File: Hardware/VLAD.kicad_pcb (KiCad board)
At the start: 2 copper layers, 90 x 90 mm, 101 parts, among them J1 BMP388, J2 BNO055, J3 Micro_SD_Card, J4 Conn_01x02_Male, J5 Conn_01x03_Male, P1 USB_C_Plug_USB2.0, Q1 S8050, Q2 S8050, Q3 S8550, Q4 S8550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

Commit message: Some connections
I hope this is ok
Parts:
- moved SW3 8.80 mm to (86.8, 106.6), turned to 180 degrees
- moved C1.4 1.62 mm to (96.4, 48.5)
- moved Battery1 1.30 mm to (92.8, 106.6), turned to 0 degrees
- moved U4 0.91 mm to (74.3, 106.9), turned to 90 degrees
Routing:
- net Net-(C2.1-Pad1): track 11.4 -> 83.2 mm
- net +3V3: track 30.8 -> 60.9 mm
- net /usb/VBUS: track 0.00 -> 24.8 mm
- net /SDCS: track 0.00 -> 15.6 mm
- net /usb/D-: track 0.00 -> 13.0 mm
- net /usb/D+: track 0.00 -> 12.3 mm
- net Net-(SW3-Pad2): track 0.00 -> 7.85 mm
- net Net-(R16-Pad2): track 0.00 -> 6.61 mm
- net Net-(Battery1-Pad1): track 0.00 -> 6.07 mm
- net /SerialRx: track 0.00 -> 5.24 mm
- net Net-(Q3-Pad1): track 0.00 -> 4.17 mm
- net Net-(Q3-Pad2): track 0.00 -> 4.04 mm
- net /USB_RTS: track 3.07 -> 7.01 mm
- net Net-(12VBoostConverter1-Pad5): track 0.00 -> 2.95 mm
- net Net-(P1-PadA5): track 0.00 -> 2.71 mm
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
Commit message: Added lots of things - needs some redoing
Fun, but ffs could have been easier
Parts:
- removed the Q5 at (82.0, 39.0)
- removed the Q6 at (82.0, 82.0)
- removed SW3: SW_SPST, Button_Switch_THT:SW_DIP_SPSTx01_Slide_9.78x4.72mm_W7.62mm_P2.54mm
- added J6: Conn_01x02_Male, Connector_PinHeader_2.54mm:PinHeader_1x02_P2.54mm_Vertical, F.Cu at (93.0, 101.0)
- added JP1: Jumper_2_Open, Connector_PinHeader_2.54mm:PinHeader_1x02_P2.54mm_Vertical, F.Cu at (74.0, 25.0)
- Q5, Q6: footprint Package_TO_SOT_THT:TO-220-3_Vertical -> Package_TO_SOT_SMD:SOT-23
- Q7: value 2N2219 -> Q_NMOS_GDS; footprint Package_TO_SOT_THT:TO-92_Inline -> Package_TO_SOT_SMD:SOT-23
- moved J2 61.4 mm to (74.0, 128.0)
- moved J1 49.3 mm to (74.0, 133.0), turned to 90 degrees
- moved Q7 37.2 mm to (74.0, 29.0), turned to 270 degrees
- moved TP6 28.4 mm to (33.0, 99.0), turned to 270 degrees
- moved R7 26.4 mm to (33.0, 102.0)
- moved C8 22.5 mm to (57.0, 98.0), turned to 90 degrees
- moved C7 21.6 mm to (55.0, 98.0), turned to 90 degrees
- moved AE1 15.1 mm to (57.0, 105.0), turned to 0 degrees
- moved SDLED2 14.8 mm to (34.0, 92.0), turned to 270 degrees
- moved U4 14.4 mm to (87.0, 100.0)
- moved R21 13.4 mm to (81.0, 99.0), turned to 0 degrees
- moved Q4 13.3 mm to (29.0, 92.0)
- moved Q5 11.7 mm to (87.0, 38.0)
- moved R14 10.6 mm to (32.0, 92.0), turned to 90 degrees
- moved U2 8.54 mm to (45.0, 98.0), turned to 0 degrees
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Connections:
- C2.1 pad 1: Net-(C2.1-Pad1) -> Net-(C1.1-Pad1)
- J4 pad 1: GND -> Net-(J4-Pad1)
- L2 pad 1: Net-(C2.1-Pad1) -> Net-(C1.1-Pad1)
- Q7 pad 1: Net-(C1.1-Pad1) -> 12VBusSwitch
- Q7 pad 2: 12VBusSwitch -> Net-(JP1-Pad1)
- Q7 pad 3: Net-(C2.1-Pad1) -> GND
- R21 pad 2: Net-(C2.1-Pad1) -> Net-(C1.1-Pad1)
- U4 pad 5: Net-(C2.1-Pad1) -> Net-(C1.1-Pad1)
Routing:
- net Net-(C2.1-Pad1): track 83.2 -> 0.00 mm
- net Net-(C1.1-Pad1): track 21.1 -> 72.2 mm
- net +3V3: track 60.9 -> 38.5 mm
- net Net-(D2-Pad2): track 21.4 -> 0.00 mm
- net Net-(D3-Pad2): track 20.8 -> 0.00 mm
- net +12V: track 46.1 -> 27.2 mm
- net /SDA: track 17.8 -> 0.00 mm
- net /SCL: track 18.5 -> 1.25 mm
- net Net-(6VBoostConverter1-Pad8): track 16.4 -> 0.00 mm
- net Net-(12VBoostConverter1-Pad8): track 16.4 -> 0.00 mm
- net /Power/Source2: track 0.00 -> 16.4 mm
- net /Power/Drain1: track 0.00 -> 15.9 mm
- net /Power/Source1: track 0.00 -> 15.0 mm
- net /Power/Drain2: track 0.00 -> 13.2 mm
- net Net-(Q4-Pad2): track 0.00 -> 8.34 mm
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
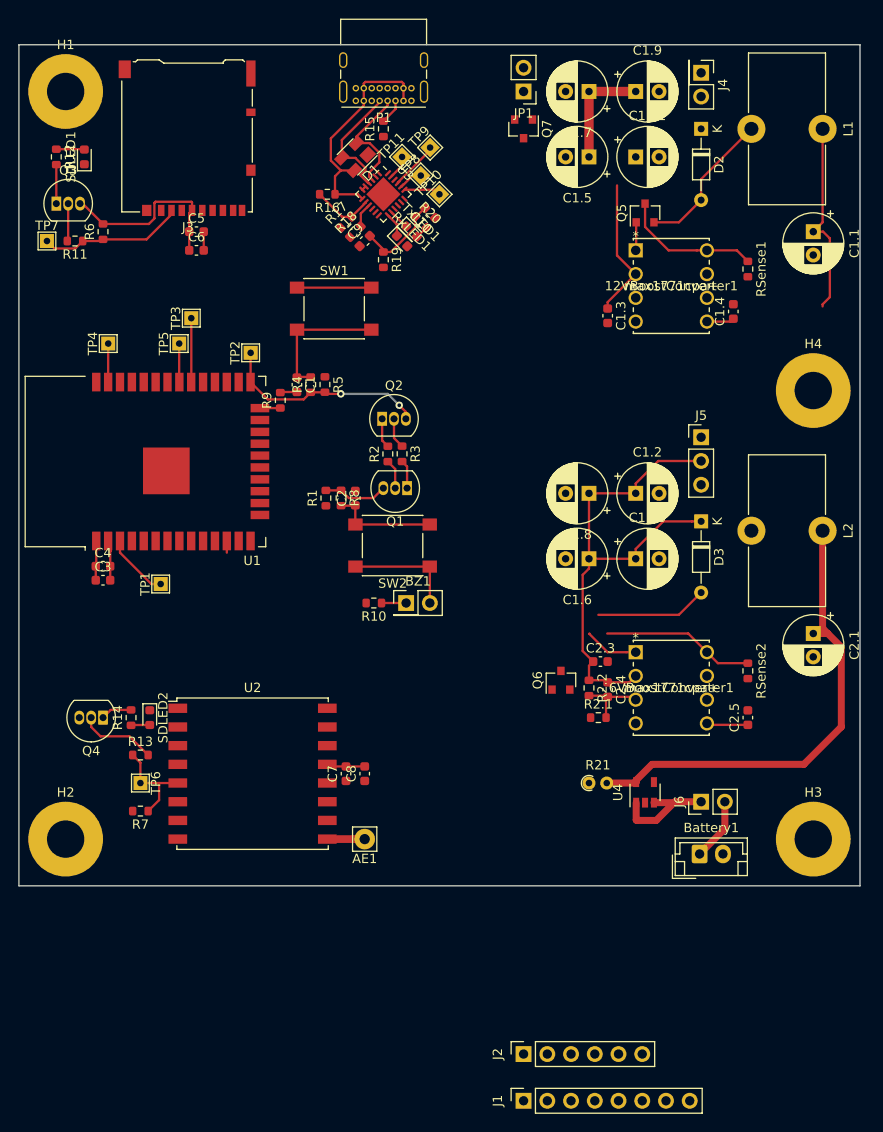
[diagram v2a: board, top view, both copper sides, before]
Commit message: Added bunch of vias
Now need to connect some more tracks up and we're good to proceed to adding ground planes etc. Also decreased the size of the board to fit within 90mm x 80mm, have further opportunities to potentially squeeze it.
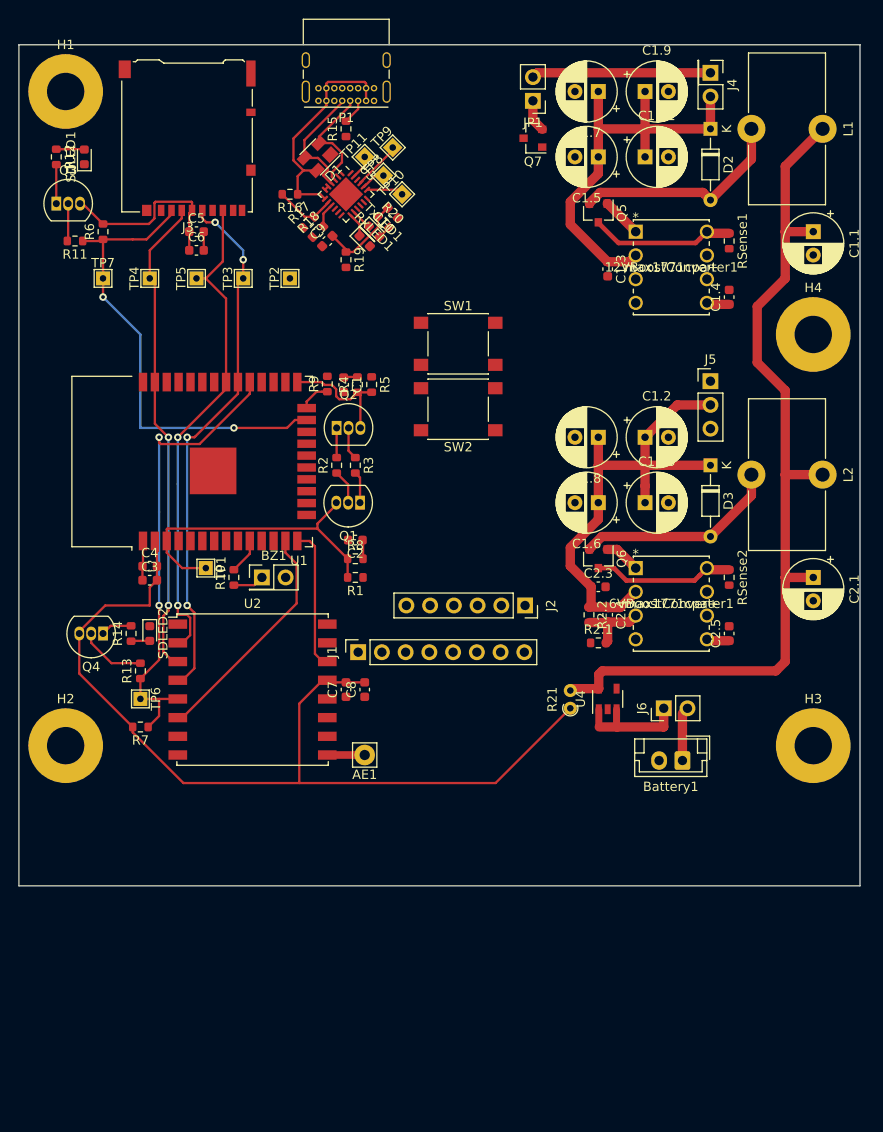
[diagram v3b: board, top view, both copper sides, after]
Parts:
- Q5, Q6: value MTP3055VL -> Q_NMOS_GDS
- moved J1 51.2 mm to (56.3, 85.0)
- moved J2 48.0 mm to (74.2, 80.0), turned to 270 degrees
- moved SW2 16.2 mm to (67.0, 59.0)
- moved BZ1 15.7 mm to (46.0, 77.0)
- moved R10 15.2 mm to (43.0, 77.0), turned to 90 degrees
- moved SW1 13.8 mm to (67.0, 52.0)
- moved Q6 13.6 mm to (82.0, 75.0), turned to 270 degrees
- moved J6 10.8 mm to (89.0, 91.0)
- moved U4 10.8 mm to (83.0, 90.0)
- moved RSense2 10.2 mm to (96.0, 77.0)
- moved Battery1 10.2 mm to (91.0, 96.6), turned to 180 degrees
- moved H2 10.0 mm to (25.0, 95.0)
- moved H3 10.0 mm to (105.0, 95.0)
- moved C2.5 9.22 mm to (96.0, 83.0)
- moved R1 9.06 mm to (56.0, 77.0), turned to 180 degrees
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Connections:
- net /Power/Drain1 renamed Net-(D2-Pad2)
- net /Power/Drain2 renamed Net-(D3-Pad2)
- net /Power/Gate1 renamed Net-(12VBoostConverter1-Pad1)
- net /Power/Gate2 renamed Net-(6VBoostConverter1-Pad1)
- net /Power/Source1 renamed Net-(12VBoostConverter1-Pad8)
- net /Power/Source2 renamed Net-(6VBoostConverter1-Pad8)
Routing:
- net +3V3: track 38.5 -> 128.3 mm
- net /SCLK: track 7.34 -> 56.9 mm, vias 0 -> 4
- net /MISO: track 4.13 -> 53.1 mm, vias 0 -> 2
- net /MOSI: track 4.63 -> 52.2 mm, vias 0 -> 2
- net /RadioCS: track 10.9 -> 50.2 mm, vias 0 -> 2
- net /SDCS: track 15.6 -> 51.1 mm, vias 0 -> 2
- net /RadioReset: track 0.00 -> 25.0 mm
- net Net-(C1.1-Pad1): track 72.2 -> 96.3 mm
- net GND: track 27.8 -> 6.71 mm
- net /EN: track 14.7 -> 34.5 mm
- net +12V: track 27.2 -> 46.9 mm
- net Net-(J4-Pad1): track 0.00 -> 19.2 mm
- net /RadioDone: track 0.50 -> 15.3 mm
- net Net-(C1-Pad1): track 14.5 -> 1.45 mm
- net Net-(C2-Pad1): track 11.5 -> 2.02 mm
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
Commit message: Not much new
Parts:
- moved J2 33.9 mm to (66.6, 113.0)
- moved J1 33.1 mm to (53.3, 118.0)
- moved SW1 10.0 mm to (57.0, 51.0)
- moved TP10 8.94 mm to (69.0, 32.0)
- moved SW2 8.06 mm to (68.0, 51.0), turned to 0 degrees
- moved TP8 6.32 mm to (65.0, 32.0)
- moved TP9 1.41 mm to (61.0, 32.0)
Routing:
- net +3V3: track 128.3 -> 236.4 mm, vias 0 -> 2
- net /USB_RTS: track 7.33 -> 65.3 mm, vias 0 -> 2
- net /SerialTx: track 2.58 -> 51.9 mm, vias 0 -> 2
- net /USB_DTR: track 6.62 -> 53.7 mm, vias 0 -> 2
- net /SerialRx: track 5.24 -> 43.7 mm, vias 0 -> 2
- net Net-(C2-Pad1): track 2.02 -> 32.7 mm
- net /IO0: track 13.7 -> 25.1 mm
- net Net-(C1-Pad1): track 1.45 -> 10.6 mm
- net Net-(R19-Pad2): track 0.00 -> 3.50 mm

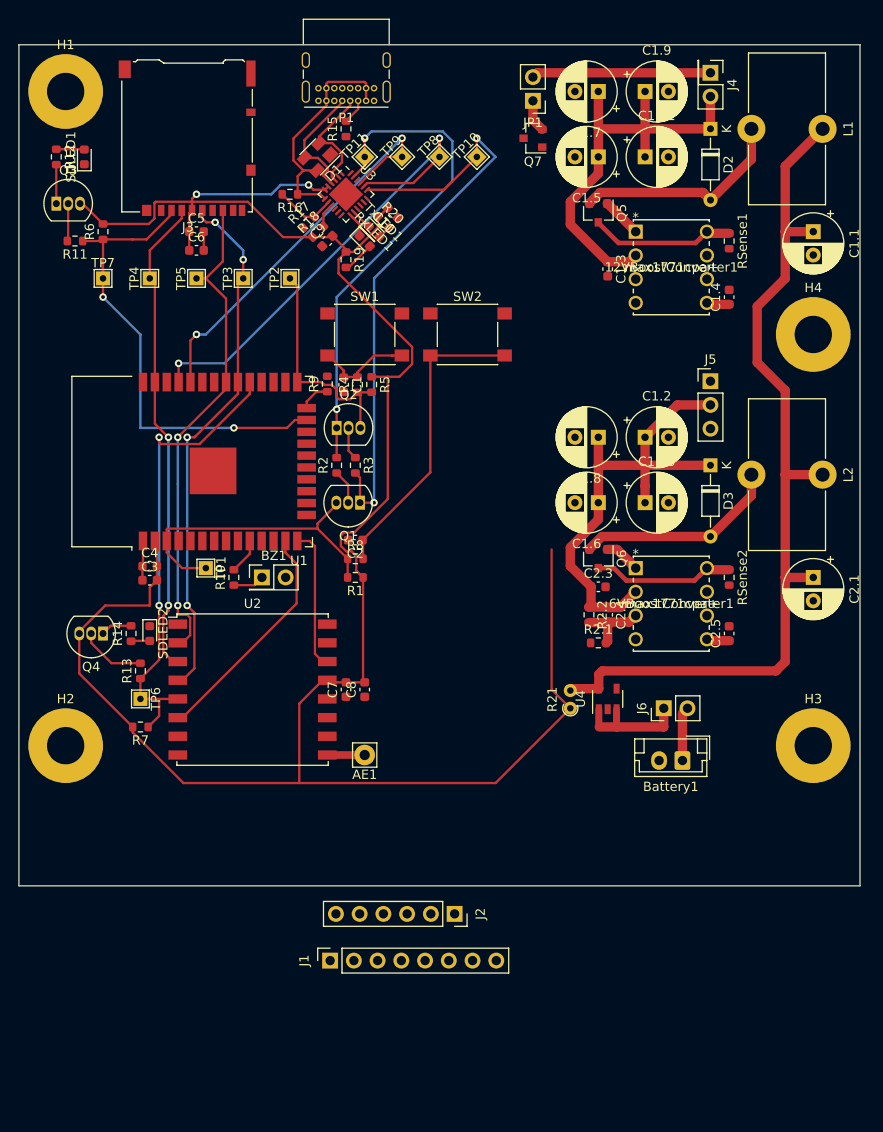
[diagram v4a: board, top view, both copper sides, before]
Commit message: Tracks done (albeit OCDifying)
All tracks are done in the sense that everything has found a routing, some components still may need to be moved though, such as the sensors on board and the push switches. 
Antenna stuff needs doing.
Board may need to be reshaped (keepout zone?).
GND plane needs to be added + silkscreens + memes
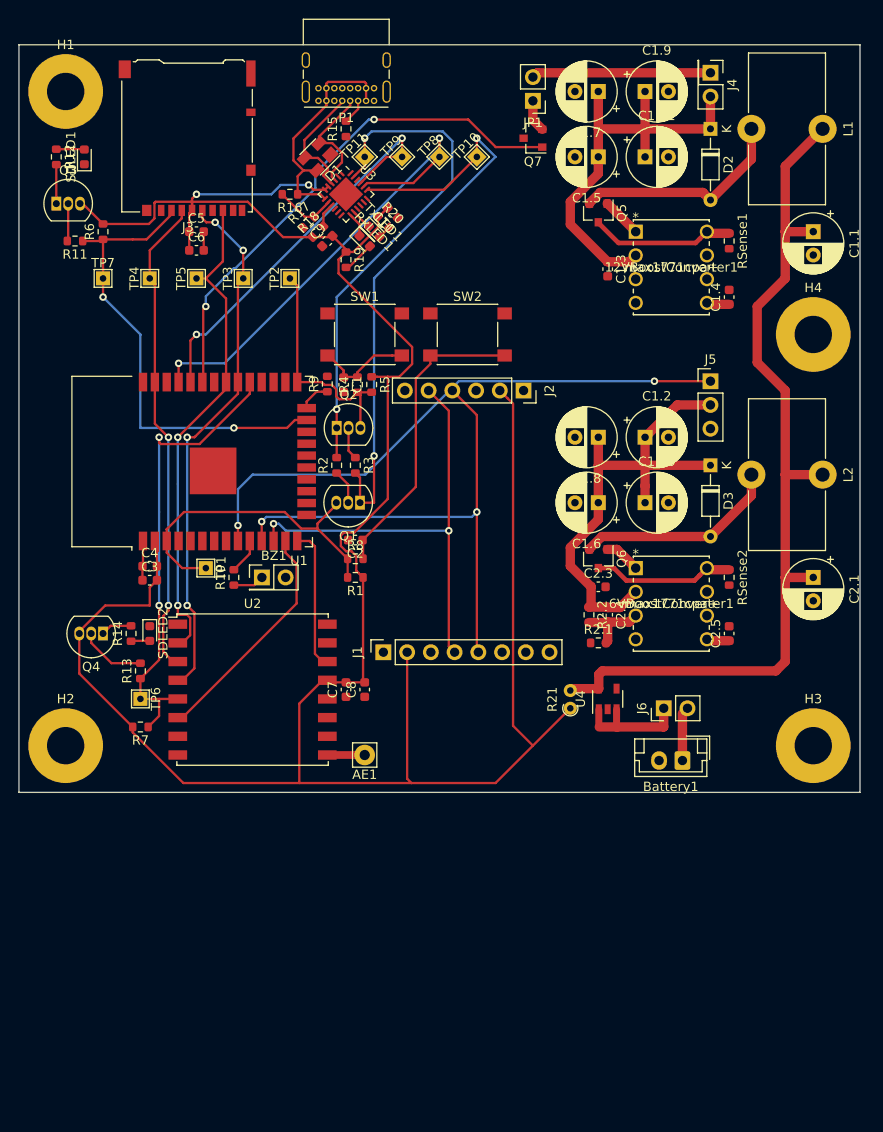
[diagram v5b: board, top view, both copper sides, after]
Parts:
- moved J2 56.5 mm to (74.0, 57.0)
- moved J1 33.5 mm to (59.0, 85.0)
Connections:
- U1 pad 33: /ServoPin -> 12VBusSwitch
- U1 pad 9: 12VBusSwitch -> /ServoPin
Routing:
- net /ServoPin: track 0.00 -> 60.9 mm, vias 0 -> 2
- net 12VBusSwitch: track 0.00 -> 55.4 mm, vias 0 -> 2
- net /SDA: track 0.00 -> 54.7 mm, vias 0 -> 2
- net /SCL: track 0.00 -> 50.1 mm, vias 0 -> 2
- net +3V3: track 236.4 -> 272.2 mm
- net /EN: track 34.5 -> 36.0 mm
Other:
- board size 90 x 90 mm -> 90 x 80 mm

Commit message: Added GND plane and 3V3 plane
4 connections left to make, not sure what the issue is with some of them...
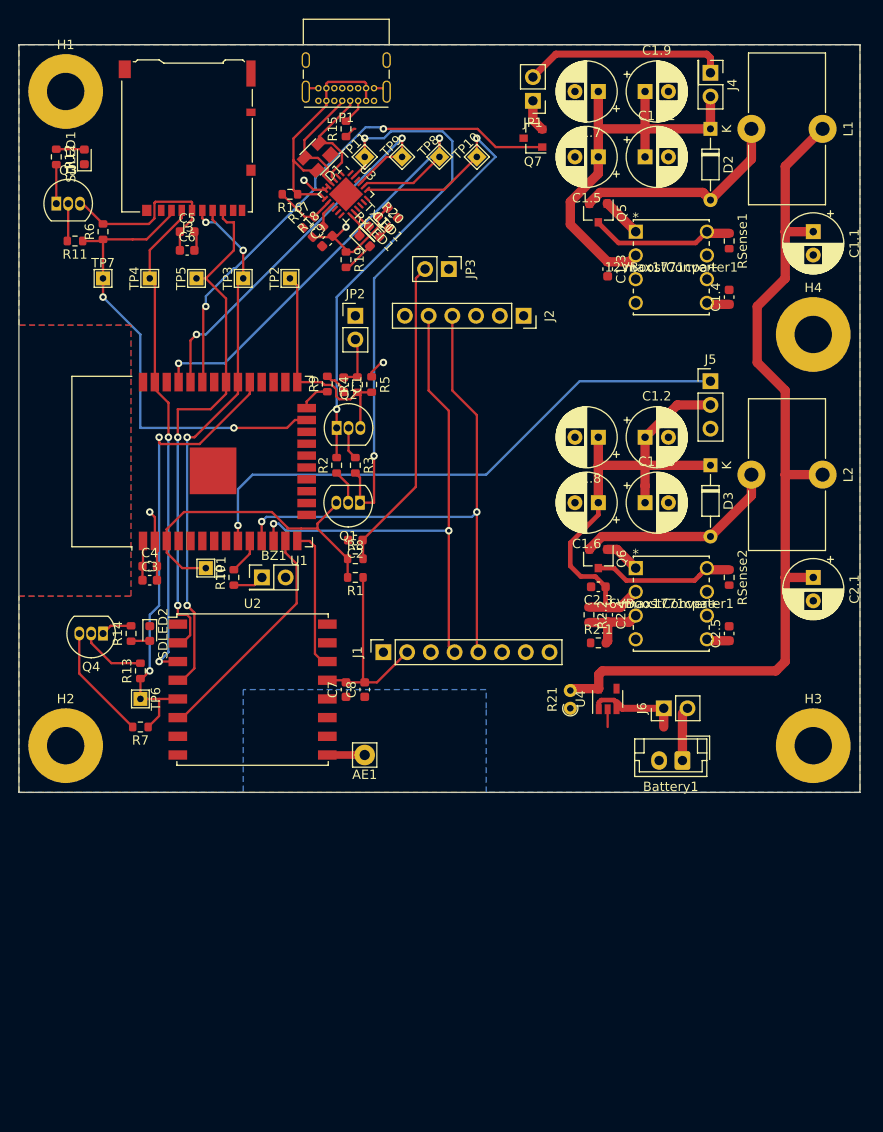
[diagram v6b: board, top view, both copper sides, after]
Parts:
- removed SW1, SW2: SW_Push, Button_Switch_SMD:SW_Push_1P1T_NO_6x6mm_H9.5mm
- added JP2: Jumper_2_Open, Connector_PinHeader_2.54mm:PinHeader_1x02_P2.54mm_Vertical, F.Cu at (56.0, 49.0)
- added JP3: Jumper_2_Open, Connector_PinHeader_2.54mm:PinHeader_1x02_P2.54mm_Vertical, F.Cu at (66.0, 44.0)
- moved J2 8.00 mm to (74.0, 49.0)
- moved C5 1.00 mm to (38.0, 40.0)
- moved C6 1.00 mm to (38.0, 42.0)
- turned C2.3 to 180 degrees
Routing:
- net +3V3: track 272.2 -> 81.2 mm, vias 2 -> 4
- net GND: track 6.71 -> 17.0 mm
- net /SDA: track 54.7 -> 62.7 mm
- net /SCL: track 50.1 -> 58.1 mm
- net Net-(C1-Pad1): track 10.6 -> 5.54 mm
- net /MISO: track 53.1 -> 57.3 mm
- net Net-(J4-Pad1): track 19.2 -> 21.8 mm
- net Net-(J6-Pad1): track 12.9 -> 11.0 mm
- net /MOSI: track 52.2 -> 53.9 mm
- net +6V: track 53.6 -> 55.2 mm
- net Net-(C2-Pad1): track 32.7 -> 33.8 mm
- net 12VBusSwitch: track 55.4 -> 54.3 mm
- net /usb/VBUS: track 24.8 -> 25.8 mm
- net /ServoPin: vias 2 -> 1
- added copper zone on B.Cu, net +3V3
- added copper zone on F.Cu, net GND

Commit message: Fixed all tracks
yay
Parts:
- moved R16 2.00 mm to (47.0, 36.0), turned to 270 degrees
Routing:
- net +3V3: track 81.2 -> 105.8 mm
- net GND: track 17.0 -> 26.3 mm
- net /usb/D-: track 13.0 -> 17.1 mm, vias 0 -> 2
- net /usb/VBUS: track 25.8 -> 29.4 mm
- net /usb/D+: track 12.3 -> 11.1 mm
- net Net-(R16-Pad2): track 6.61 -> 7.45 mm
